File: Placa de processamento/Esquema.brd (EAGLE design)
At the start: 145.1 x 89.8 mm, 14 parts

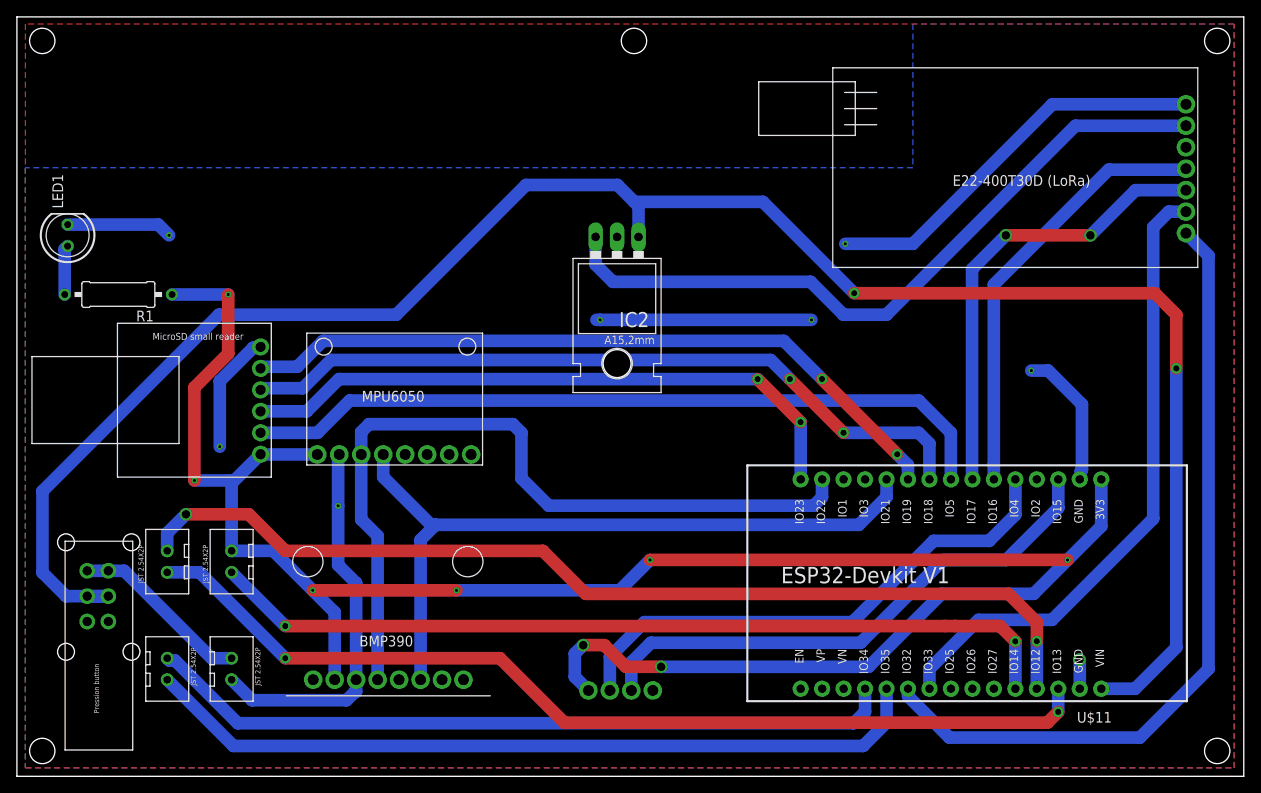
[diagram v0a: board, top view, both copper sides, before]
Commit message: Adiciona Placa de processamento ao repositório
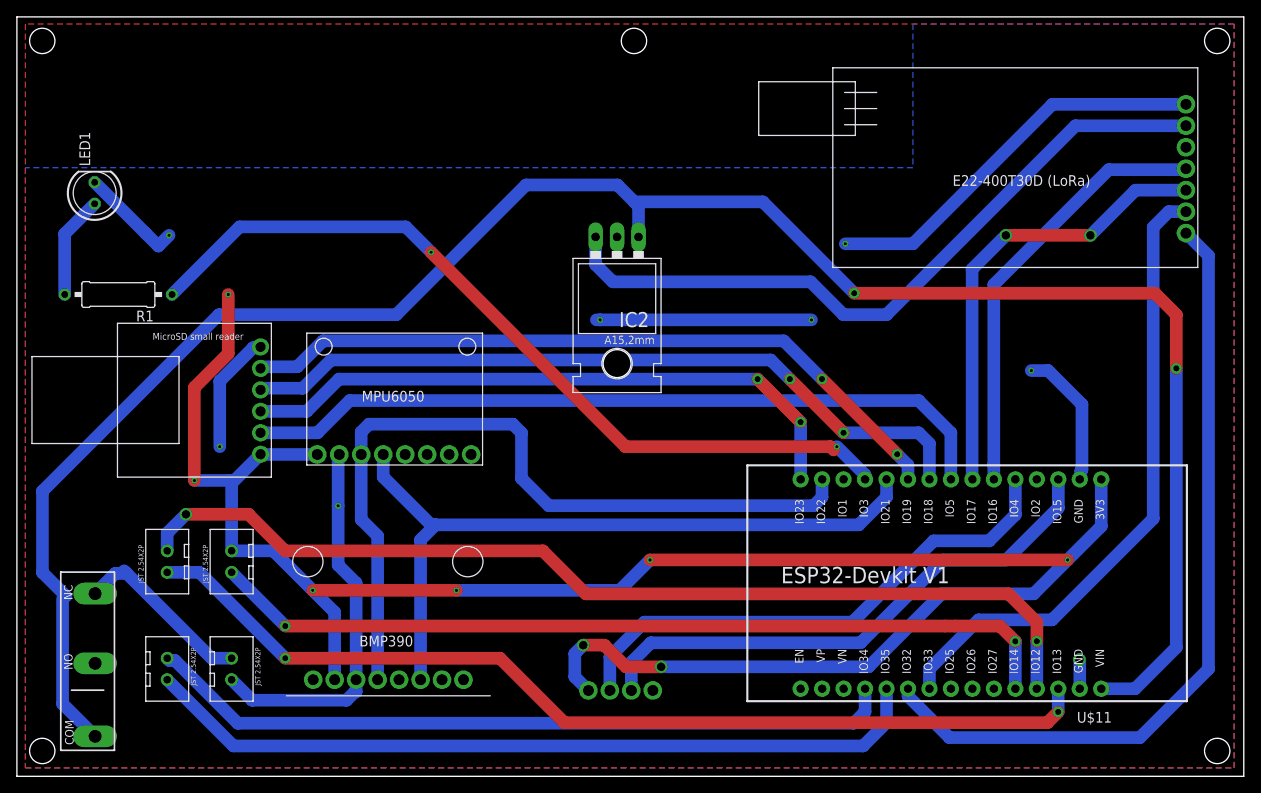
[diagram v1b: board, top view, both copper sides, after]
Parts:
- removed U$10: PRESSION_BUTTON, CRD:PRESSION_BUTTON_FOOTPRINT
- added U$12: CHAVE_SS-5GL, CRD:CHAVESS-5GL
- moved LED1 5.94 mm to (9.20, 69.0)
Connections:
- new net N$17: R1.1, U$11.12
- net N$3: no longer R1.1
- net N$7: now also U$12.P$1; no longer U$10.PL2, U$10.PR2
- net V_BATTERY: now also U$12.P$3; no longer U$10.PL1, U$10.PR1
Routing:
- net N$17: track 0.00 -> 97.8 mm, vias 0 -> 2
- net N$7: track 231.2 -> 241.6 mm
- net N$3: track 249.6 -> 242.9 mm
- net N$4: track 5.87 -> 12.2 mm
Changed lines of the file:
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@@
 </class>
 </classes>
-<designrules name="default">
+<designrules name="padronizacao do eagle">
 <description language="de">&lt;b&gt;EAGLE Design Rules&lt;/b&gt;
 &lt;p&gt;
@@
 <elements>
 <element name="U$1" library="CRD" library_urn="urn:adsk.eagle:library:39051337" package="BMP390_FOOTPRINT" package3d_urn="urn:adsk.eagle:package:40965124/5" value="BMP390V1" x="43.561" y="19.812" smashed="yes"/>
-<element name="U$10" library="CRD" library_urn="urn:adsk.eagle:library:39051337" package="PRESSION_BUTTON_FOOTPRINT" package3d_urn="urn:adsk.eagle:package:43483815/3" value="PRESSION_BUTTON" x="9.62" y="16.51" smashed="yes" rot="R270"/>
-<element name="U$2" library="CRD" library_urn="urn:adsk.eagle:library:39051337" package="E22-400T30D_FOOTPRINT" package3d_urn="urn:adsk.eagle:package:40965099/4" value="E22-400T30D" x="121.92" y="73.66" smashed="yes" rot="R180"/>
-<element name="U$3" library="CRD" library_urn="urn:adsk.eagle:library:39051337" package="GPS_MODULE_FOOTPRINT" package3d_urn="urn:adsk.eagle:package:39608400/5" value="GPS_MODULE" x="71.22" y="26.67" smashed="yes" rot="MR0"/>
+<element name="U$2" library="CRD" library_urn="urn:adsk.eagle:library:39051337" package="E22-400T30D_FOOTPRINT" package3d_urn="urn:adsk.eagle:package:40965099/5" value="E22-400T30D" x="121.92" y="73.66" smashed="yes" rot="R180"/>
+<element name="U$3" library="CRD" library_urn="urn:adsk.eagle:library:39051337" package="GPS_MODULE_FOOTPRINT" package3d_urn="urn:adsk.eagle:package:39608400/7" value="GPS_MODULE" x="71.22" y="26.67" smashed="yes" rot="MR0"/>
 <element name="U$4" library="CRD" library_urn="urn:adsk.eagle:library:39051337" package="JST2.54X2P_FOOTPRINT" package3d_urn="urn:adsk.eagle:package:39191967/2" value="JST2.54X2P" x="25.4" y="25.4" smashed="yes" rot="R90"/>
 <element name="U$5" library="CRD" library_urn="urn:adsk.eagle:library:39051337" package="JST2.54X2P_FOOTPRINT" package3d_urn="urn:adsk.eagle:package:39191967/2" value="JST2.54X2P" x="17.78" y="12.7" smashed="yes" rot="R270"/>
@@
 <attribute name="VALUE" x="74.937" y="57.46" size="1.778" layer="27" ratio="10" rot="R180"/>
 </element>
-<element name="LED1" library="led" library_urn="urn:adsk.eagle:library:259" package="LED5MM" package3d_urn="urn:adsk.eagle:package:15799/2" value="" x="6" y="64" smashed="yes" rot="R90">
-<attribute name="NAME" x="5.4666" y="67.175" size="1.27" layer="25" ratio="10" rot="R90"/>
-<attribute name="POPULARITY" value="93" x="6" y="64" size="1.778" layer="27" rot="R90" display="off"/>
-<attribute name="VALUE" x="7.8034" y="67.2004" size="1.27" layer="27" ratio="10" rot="R90"/>
+<element name="LED1" library="led" library_urn="urn:adsk.eagle:library:259" package="LED5MM" package3d_urn="urn:adsk.eagle:package:15799/2" value="" x="9.2" y="69" smashed="yes" rot="R90">
+<attribute name="NAME" x="8.6666" y="72.175" size="1.27" layer="25" ratio="10" rot="R90"/>
+<attribute name="POPULARITY" value="93" x="9.2" y="69" size="1.778" layer="27" rot="R90" display="off"/>
+<attribute name="VALUE" x="11.0034" y="72.2004" size="1.27" layer="27" ratio="10" rot="R90"/>
 </element>
 <element name="R1" library="rcl" library_urn="urn:adsk.eagle:library:334" package="0309/12" package3d_urn="urn:adsk.eagle:package:23571/1" value="" x="12" y="57" smashed="yes" rot="R180">
@@
 <attribute name="VALUE" x="15.175" y="57.6858" size="1.27" layer="27" ratio="10" rot="R180"/>
 </element>
+<element name="U$12" library="CRD" library_urn="urn:adsk.eagle:library:39051337" package="CHAVESS-5GL" package3d_urn="urn:adsk.eagle:package:45208058/6" value="CHAVE_SS-5GL" x="9" y="14" smashed="yes" rot="R90"/>
 </elements>
 <signals>
@@
 <wire x1="66" y1="11.77" x2="67.61" y2="10.16" width="1.5" layer="16"/>
 <wire x1="66" y1="14.518" x2="66" y2="11.77" width="1.5" layer="16"/>
-<contactref element="R1" pad="1"/>
-<wire x1="18.35" y1="57" x2="25" y2="57" width="1.5" layer="16"/>
 <via x="25" y="57" extent="1-16" drill="0.35"/>
 <wire x1="25.4" y1="34.671" x2="25.071" y2="35" width="1.5" layer="16"/>
@@
 <wire x1="88.25" y1="67.96" x2="73.04" y2="67.96" width="1.5" layer="16"/>
 <wire x1="71.04" y1="69.96" x2="60.23" y2="69.96" width="1.5" layer="16"/>
-<wire x1="10.818" y1="21.313" x2="5.818" y2="21.313" width="1.5" layer="16"/>
 <wire x1="5.818" y1="21.313" x2="3.023" y2="24.108" width="1.5" layer="16"/>
 <wire x1="3.023" y1="33.733" x2="3.023" y2="24.108" width="1.5" layer="16"/>
 <wire x1="44.88" y1="54.61" x2="60.23" y2="69.96" width="1.5" layer="16"/>
-<contactref element="U$10" pad="PR2"/>
-<contactref element="U$10" pad="PL2"/>
-<wire x1="8.318" y1="21.313" x2="10.818" y2="21.313" width="1.5" layer="16"/>
 <contactref element="IC2" pad="IN"/>
 <wire x1="73.54" y1="63.81" x2="73.54" y2="67.46" width="1.5" layer="16"/>
 <wire x1="73.54" y1="67.46" x2="73.04" y2="67.96" width="1.5" layer="16"/>
 <wire x1="73.04" y1="67.96" x2="71.04" y2="69.96" width="1.5" layer="16"/>
+<contactref element="U$12" pad="P$1"/>
+<wire x1="9.254" y1="4.729" x2="5.4052" y2="8.5778" width="1.5" layer="16"/>
+<wire x1="5.4052" y1="8.5778" x2="5.4052" y2="21" width="1.5" layer="16"/>
+<wire x1="5.4052" y1="21" x2="5.818" y2="21.313" width="0" layer="19" extent="16-16"/>
 </signal>
 <signal name="N$12">
@@
 <signal name="V_BATTERY">
 <contactref element="U$7" pad="1"/>
-<contactref element="U$10" pad="PR1"/>
-<contactref element="U$10" pad="PL1"/>
-<wire x1="8.318" y1="24.313" x2="10.818" y2="24.313" width="1.5" layer="16"/>
-<wire x1="10.818" y1="24.313" x2="12.687" y2="24.313" width="1.5" layer="16"/>
 <wire x1="23.03" y1="13.97" x2="25.4" y2="13.97" width="1.5" layer="16"/>
-<wire x1="12.687" y1="24.313" x2="23.03" y2="13.97" width="1.5" layer="16"/>
+<wire x1="12.687" y1="24.313" x2="13" y2="24" width="1.5" layer="16"/>
+<contactref element="U$12" pad="P$3"/>
+<wire x1="13" y1="24" x2="23.03" y2="13.97" width="1.5" layer="16"/>
+<wire x1="9.254" y1="21.62" x2="11.634" y2="24" width="1.5" layer="16"/>
+<wire x1="11.634" y1="24" x2="13" y2="24" width="1.5" layer="16"/>
 </signal>
 <signal name="N$19">
@@
 </polygon>
 <contactref element="LED1" pad="K"/>
-<wire x1="6" y1="65.27" x2="16.73" y2="65.27" width="1.5" layer="16"/>
-<wire x1="16.73" y1="65.27" x2="18" y2="64" width="1.5" layer="16"/>
+<wire x1="18" y1="64" x2="16.735" y2="62.735" width="1.5" layer="16"/>
+<wire x1="9.2" y1="70.27" x2="15.235" y2="64.235" width="1.5" layer="16"/>
 <via x="18" y="64" extent="1-16" drill="0.35"/>
+<wire x1="15.235" y1="64.235" x2="16.735" y2="62.735" width="1.5" layer="16"/>
+<wire x1="15.235" y1="64.235" x2="15.235" y2="64.235" width="1.5" layer="16"/>
 </signal>
 <signal name="N$4">
 <contactref element="R1" pad="2"/>
 <contactref element="LED1" pad="A"/>
-<wire x1="5.65" y1="57" x2="5.65" y2="62.38" width="1.5" layer="16"/>
-<wire x1="5.65" y1="62.38" x2="6" y2="62.73" width="1.5" layer="16"/>
+<wire x1="5.65" y1="57" x2="5.65" y2="64.18" width="1.5" layer="16"/>
+<wire x1="5.65" y1="64.18" x2="9.2" y2="67.73" width="1.5" layer="16"/>
+</signal>
+<signal name="N$17">
+<contactref element="R1" pad="1"/>
+<contactref element="U$11" pad="12"/>
+<wire x1="18.35" y1="57" x2="26.35" y2="65" width="1.5" layer="16"/>
+<wire x1="46" y1="65" x2="49" y2="62" width="1.5" layer="16"/>
+<via x="49" y="62" extent="1-16" drill="0.35"/>
+<wire x1="49" y1="62" x2="72" y2="39" width="1.5" layer="1"/>
+<via x="97" y="39" extent="1-16" drill="0.35"/>
+<wire x1="96.23104375" y1="39" x2="96.615521875" y2="38.615521875" width="1.5" layer="1"/>
+<wire x1="26.35" y1="65" x2="46" y2="65" width="1.5" layer="16"/>
+<wire x1="72" y1="39" x2="96.23104375" y2="39" width="1.5" layer="1"/>
+<wire x1="97" y1="39" x2="100.34" y2="35.66" width="1.5" layer="16"/>
+<wire x1="100.34" y1="35.66" x2="100.34" y2="35.13" width="1.5" layer="16"/>
+<wire x1="96.615521875" y1="38.615521875" x2="97" y2="39" width="0" layer="19" extent="1-1"/>
 </signal>
 </signals>

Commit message: Coisas
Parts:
- added R2: 40R, rcl:0309/12
- IC2: value (none) -> 5V
- LED1: value (none) -> RED
- R1: value (none) -> 220R
- moved U$6 115.2 mm to (131.6, 7.78), turned to 180 degrees
- moved U$5 104.5 mm to (122.2, 7.82), turned to 180 degrees
- moved IC2 70.2 mm to (17.6, 14.4), turned to 0 degrees
- moved LED1 35.1 mm to (7.20, 34.0)
- moved R1 23.8 mm to (18.0, 34.0)
- moved U$2 10.0 mm to (121.9, 63.7)
- moved U$11 7.00 mm to (105.4, 28.6)
- moved U$12 5.10 mm to (8.00, 19.0)
- moved U$7 3.77 mm to (27.4, 15.9), turned to 90 degrees
- moved U$8 3.00 mm to (21.6, 47.5)
- moved U$4 2.24 mm to (27.4, 24.4)
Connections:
- net N$1 renamed SDA
- net N$10 renamed M1
- net N$11 renamed M0
- net N$13 renamed CS
- net N$14 renamed MOSI
- net N$15 renamed CLK
- net N$16 renamed MISO
- net N$17 renamed LED1
- net N$19 renamed SKIB1
- net N$2 renamed SCL
- net N$20 renamed SKIB2
- net N$21 renamed BUZZER
- net N$3 renamed 3V3
- net N$5 renamed TX1
- net N$6 renamed RX1
- net N$8 renamed TX2
- net N$9 renamed RX2
- removed net N$12: IC2.OUT, U$2.VCC
- removed net N$22: U$11.19, U$5.1
- removed net N$23: U$11.20, U$5.2
- new net OPTOACOPLADOR1: U$11.20, U$5.1
- new net OPTOACOPLADOR2: U$11.19, U$5.2
- new net VIN: IC2.IN, U$12.P$1
- new net VOUT: IC2.OUT, U$11.30, U$2.VCC
- net GND: now also R2.1; no longer U$11.29, U$2.GND
- net N$7: now also R2.2, U$2.GND; no longer IC2.IN, U$11.30, U$12.P$1
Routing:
- net N$7: track 241.6 -> 8.14 mm, vias 2 -> 0
- net VOUT: track 0.00 -> 202.6 mm
- net GND: track 164.5 -> 0.00 mm, vias 8 -> 0
- net SKIB2: track 119.1 -> 16.3 mm, vias 2 -> 0
- net SKIB1: track 116.0 -> 17.1 mm, vias 2 -> 0
- net N$23: track 93.5 -> 0.00 mm
- net N$22: track 89.0 -> 0.00 mm
- net N$12: track 84.8 -> 0.00 mm
- net 3V3: track 242.9 -> 177.1 mm, vias 8 -> 0
- net M0: track 94.5 -> 64.3 mm, vias 0 -> 2
- net OPTOACOPLADOR2: track 0.00 -> 26.5 mm
- net OPTOACOPLADOR1: track 0.00 -> 26.3 mm
- net CS: track 90.3 -> 111.8 mm
- net LED1: track 97.8 -> 117.6 mm
- net TX2: track 54.1 -> 38.5 mm
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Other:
- board size 145.1 x 89.8 mm -> 145.1 x 79.8 mm
